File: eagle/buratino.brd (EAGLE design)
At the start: 25.4 x 50.8 mm, 50 parts, among them IC1 LTC3105MS, J2 AVR_SPI, J4 Ext Battery, Q2 2n7002PW, U4 ATMEGA256RFR2, U7 SWITCH, U8 LED-RGB, X1 16MHz, X2 32.768k, Y1 ANTENNA2SMD5

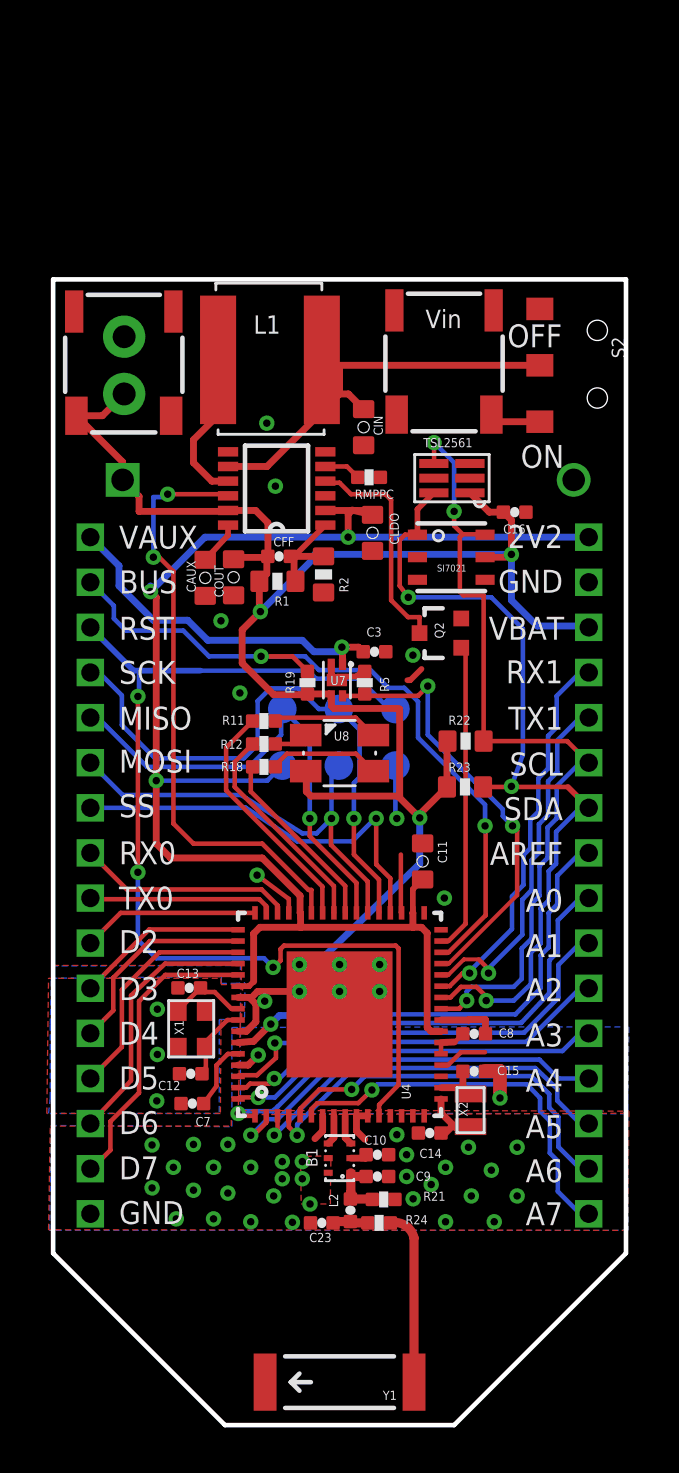
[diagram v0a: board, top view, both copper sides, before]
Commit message: replace ICSP with JTAG
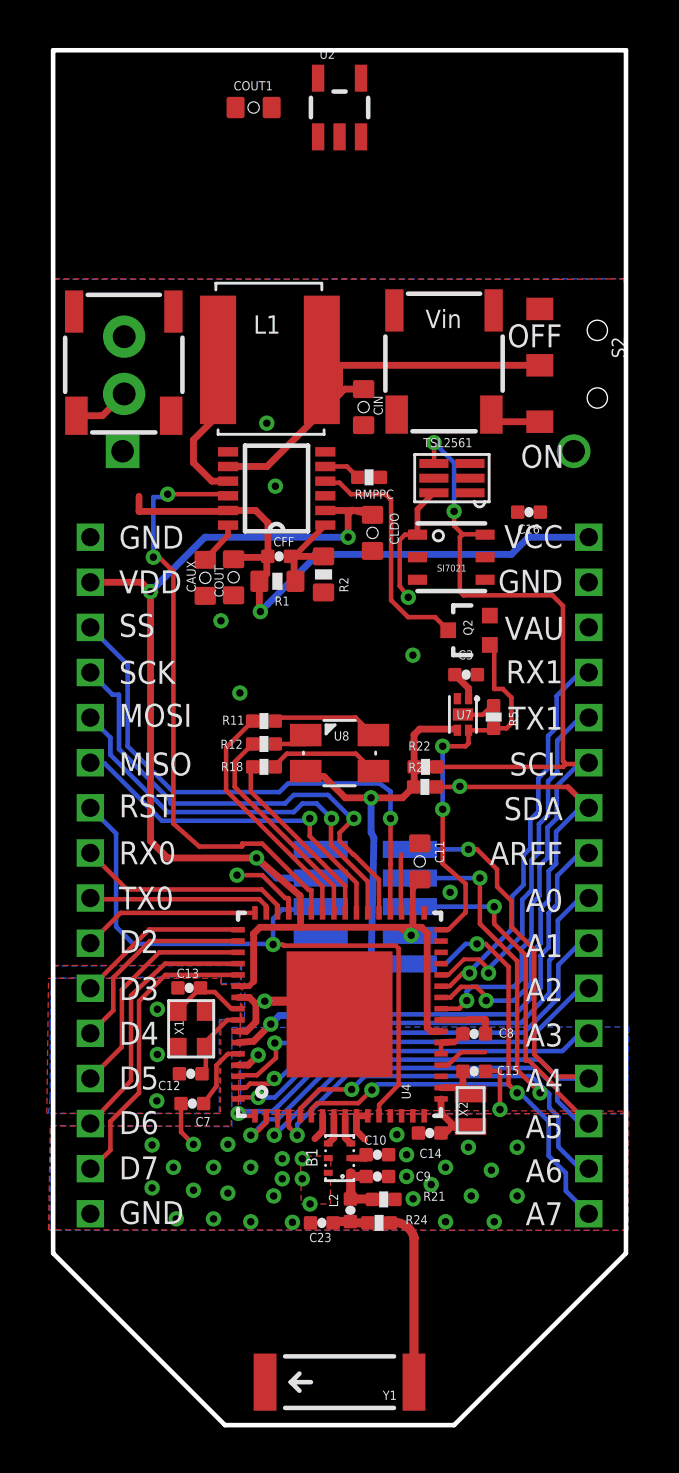
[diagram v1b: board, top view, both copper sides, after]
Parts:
- removed J2: AVR_SPI, Pinoccio:2X3-PAD
- removed R19: 2K, Pinoccio:0402-RES
- added COUT1: 1.0uF, Pinoccio:0603-CAP
- added U2: TPS78222, Pinoccio:SOT23-5
- added X3: AVR_JTAG, 620-Misc:PHB_1MM27_2X05_SNS
- R22, R23: device Pinoccio:0603-RES -> Pinoccio:0402-RES
- moved R5 5.91 mm to (19.5, 31.4)
- moved U7 5.79 mm to (18.8, 32.3)
- moved C3 4.19 mm to (18.3, 33.3)
- moved R22 2.11 mm to (16.5, 29.2)
- moved R23 1.78 mm to (16.5, 28.3)
- moved Q2 1.28 mm to (18.4, 35.2)
- moved CSTOR 1.27 mm to (13.1, 43.2)
- moved CIN 0.89 mm to (13.8, 45.1)
- moved C16 0.64 mm to (21.1, 40.5)
- moved C11 0.13 mm to (16.3, 25.0)
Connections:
- removed net BKPK-BUS: JP-L.P$2, R19.2, U4.30
- removed net BKPKVCC-EN: R5.1, U4.29, U7.P$4
- new net N$66: U2.1, U2.3
- net A4: now also X3.1
- net A5: now also X3.5
- net A6: now also X3.3
- net A7: now also X3.9
- net GND: now also COUT1.2, JP-L.P$1, U2.2, U2.4, X3.10, X3.2; no longer J2.6
- net MISO: now also JP-L.P$6; no longer J2.1, JP-L.P$5
- net MOSI: now also JP-L.P$5; no longer J2.4, JP-L.P$6
- net RESET: now also JP-L.P$7, X3.6; no longer J2.5, JP-L.P$3
- net SCK: no longer J2.3
- net SHDWN: now also R5.1, U4.29, U4.32, U7.P$4; no longer U4.31
- net SSN: now also JP-L.P$3; no longer JP-L.P$7
- net VCC: now also COUT1.1, JP-R.P$1, U2.5; no longer C16.1, JP-R.P$3, R19.1, SI7021.5, TSL2561.1
- net VCC-AE: now also C16.1, JP-R.P$3, SI7021.5, TSL2561.1; no longer JP-L.P$1
- net VDD: now also JP-L.P$2, X3.4, X3.7; no longer J2.2, JP-R.P$1
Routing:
- net BKPK-BUS: track 32.8 -> 0.00 mm, vias 2 -> 0
- net VCC: track 82.2 -> 55.7 mm, vias 4 -> 3
- net BKPKVCC-EN: track 19.7 -> 0.00 mm, vias 2 -> 0
- net RESET: track 47.6 -> 29.9 mm, vias 3 -> 1
- net A4: track 16.6 -> 32.6 mm, vias 1 -> 2
- net A5: track 16.8 -> 31.9 mm, vias 1 -> 2
- net VCC-AE: track 15.7 -> 1.32 mm, vias 1 -> 0
- net A6: track 16.5 -> 30.6 mm, vias 1 -> 3
- net SDA: track 37.8 -> 27.1 mm
- net A7: track 17.4 -> 27.7 mm, vias 1 -> 3
- net VDD: track 69.4 -> 60.9 mm, vias 3 -> 4
- net SCL: track 37.2 -> 43.3 mm
- net SSN: track 18.1 -> 24.1 mm
- net MISO: track 21.5 -> 15.9 mm
- net SCK: track 26.1 -> 21.4 mm
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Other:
- board size 25.4 x 50.8 mm -> 25.4 x 61 mm
- board text added: "Buratino v1.1"
- board text added: "VAU"
- board text added: "VCC"
- board text added: "VDD"
- board text removed: "2V2"
- board text removed: "BUS"
- board text removed: "Buratino v1.0a"
- board text removed: "VAUX"
- board text removed: "VBAT"

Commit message: replace 2mm headers with 0.1" headers
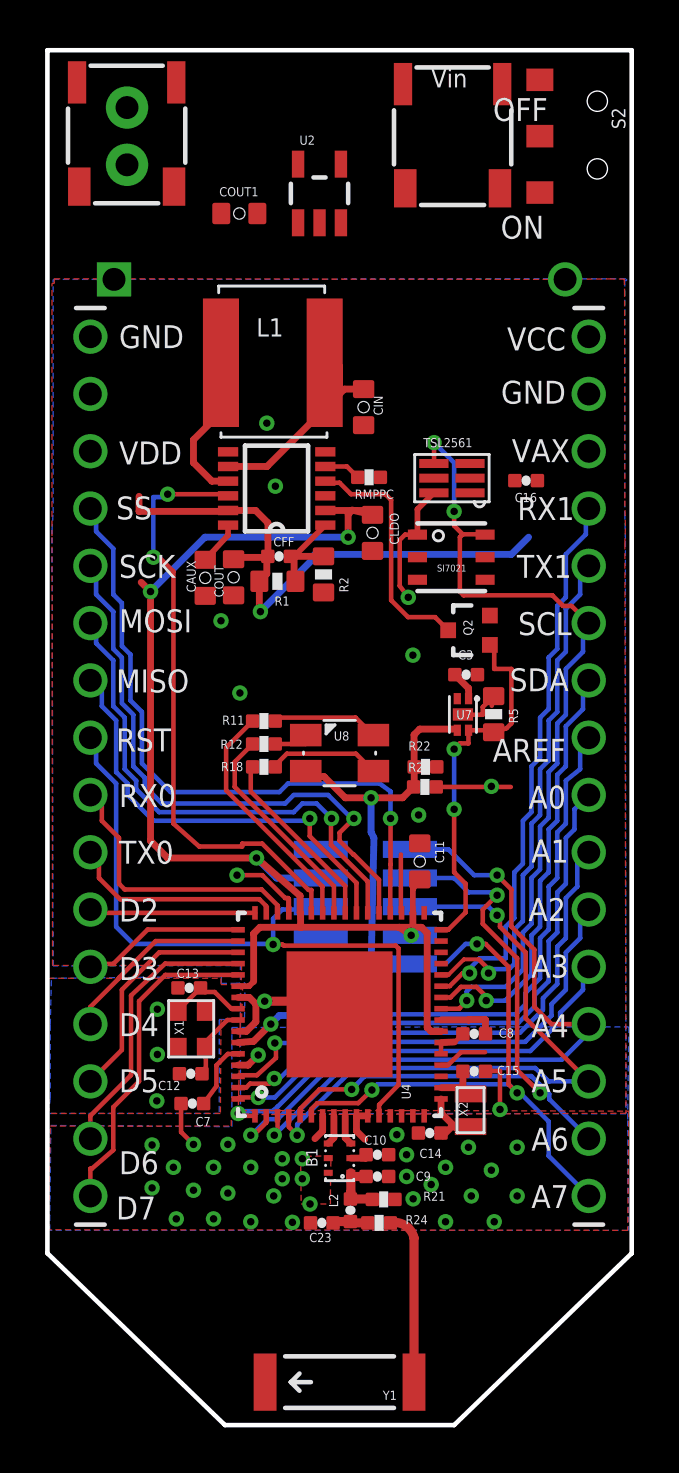
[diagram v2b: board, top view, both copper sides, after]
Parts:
- JP-L, JP-R: value M162MM -> M16PTH; device Pinoccio:1X16_2MM -> 620-Misc:1X16
- R5: device Pinoccio:0402-RES -> Pinoccio:0603-RES
- moved BATT 10.2 mm to (0.66, 60.3)
- moved J4 10.2 mm to (3.28, 58.4)
- moved S2 10.2 mm to (24.1, 57.1)
- moved PV 10.0 mm to (15.1, 60.2)
- moved JP-L 8.89 mm to (1.65, 48.3)
- moved JP-R 8.89 mm to (23.7, 48.3)
- moved CSTOR 7.63 mm to (12.7, 50.8)
- moved COUT1 4.74 mm to (8.26, 53.7)
- moved U2 3.91 mm to (11.8, 54.6)
- moved C16 1.40 mm to (21.0, 41.9)
- moved L1 0.18 mm to (9.74, 47.1)
- moved R5 0.13 mm to (19.5, 31.5)
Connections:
- new net 123: JP-L.2
- net A0: now also JP-R.9; no longer JP-R.P$9
- net A1: now also JP-R.10; no longer JP-R.P$10
- net A2: now also JP-R.11; no longer JP-R.P$11
- net A3: now also JP-R.12; no longer JP-R.P$12
- net A4: now also JP-R.13; no longer JP-R.P$13
- net A5: now also JP-R.14; no longer JP-R.P$14
- net A6: now also JP-R.15; no longer JP-R.P$15
- net A7: now also JP-R.16; no longer JP-R.P$16
- net AREF: now also JP-R.8; no longer JP-R.P$8
- net D2: now also JP-L.11; no longer JP-L.P$10
- net D3: now also JP-L.12; no longer JP-L.P$11
- net D4: now also JP-L.13; no longer JP-L.P$12
- net D5: now also JP-L.14; no longer JP-L.P$13
- net D6: now also JP-L.15; no longer JP-L.P$14
- net D7: now also JP-L.16; no longer JP-L.P$15
- net GND: now also JP-L.1, JP-R.2; no longer JP-L.P$1, JP-L.P$16, JP-R.P$2
- net MISO: now also JP-L.7; no longer JP-L.P$6
- net MOSI: now also JP-L.6; no longer JP-L.P$5
- net RESET: now also JP-L.8; no longer JP-L.P$7
- net RX0: now also JP-L.9; no longer JP-L.P$8
- net RX1: now also JP-R.4; no longer JP-R.P$4
- net SCK: now also JP-L.5; no longer JP-L.P$4
- net SCL: now also JP-R.6; no longer JP-R.P$6
- net SDA: now also JP-R.7; no longer JP-R.P$7
- net SSN: now also JP-L.4; no longer JP-L.P$3
- net TX0: now also JP-L.10; no longer JP-L.P$9
- net TX1: now also JP-R.5; no longer JP-R.P$5
- net VCC: now also JP-R.1; no longer JP-R.P$1
- net VCC-AE: now also JP-R.3; no longer JP-R.P$3
- net VDD: now also JP-L.3; no longer JP-L.P$2
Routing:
- net N$9: track 19.2 -> 9.97 mm
- net RX1: track 17.3 -> 25.0 mm
- net TX1: track 16.1 -> 23.2 mm
- net SCL: track 43.3 -> 36.6 mm
- net SSN: track 24.1 -> 29.5 mm
- net VCC: track 55.7 -> 50.5 mm
- net AREF: track 22.6 -> 27.5 mm
- net SCK: track 21.4 -> 26.1 mm
- net MOSI: track 18.2 -> 22.6 mm
- net A0: track 20.7 -> 25.0 mm
- net A1: track 19.3 -> 23.0 mm
- net MISO: track 15.9 -> 19.4 mm
- net A2: track 18.6 -> 21.9 mm
- net A5: track 31.9 -> 28.8 mm
- net RESET: track 29.9 -> 33.0 mm
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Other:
- board size 25.4 x 61 mm -> 25.9 x 61 mm
- board text added: "VAX"
- board text removed: "VAU"

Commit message: add PIR
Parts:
- removed PV: SolarCell, bean:JST-SFH
- added J1: Vcc-Vdd Tie, Pinoccio:SJ_2S-NO
- added J2: Ext Battery, Pinoccio:1X02
- added R3: 10K, Pinoccio:0603-RES
- added R4: 47K, Pinoccio:0603-RES
- added S1: (no value), SparkFun-Electromechanical:TACTILE-PTH
- added U$1: IRS-B210ST01R1, 620-Sensors:PIRSMT
- added VIN1: Ext Power, bean:JST-SFH
- BATT: value JST Bat -> Aux Bat
- J4: value Ext Battery -> Aux Batt
- R11, R12, R18, R22, R23: device Pinoccio:0402-RES -> Pinoccio:0603-RES
- moved COUT1 8.50 mm to (9.65, 45.3), turned to 180 degrees
- moved U2 6.91 mm to (9.78, 48.0), turned to 180 degrees
- moved S2 1.40 mm to (24.0, 55.8)
- moved BATT 1.17 mm to (0.41, 59.1)
- moved CIN 1.02 mm to (13.8, 44.1)
- moved J4 0.92 mm to (3.02, 57.5)
- moved R22 0.74 mm to (16.9, 29.8)
- moved R11 0.65 mm to (8.71, 31.3)
- moved R12 0.64 mm to (8.71, 30.2)
- moved R23 0.54 mm to (16.9, 28.7)
- moved R18 0.52 mm to (8.84, 29.1)
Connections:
- removed net 123: JP-L.2
- removed net N$66: U2.1, U2.3
- removed net N$9: CIN.1, IC1.8, L1.P$1, S2.2
- new net BTN: R3.2, S1.3, S1.4, U4.32
- new net VIN: CIN.1, IC1.8, L1.P$1, S2.2, U2.1, U2.3
- net A0: now also R4.1, U$1.VOUT
- net GND: now also J2.1, R4.2, S1.1, S1.2, U$1.GND, U$1.GND*1, U$1.GND*2, VIN1.2; no longer PV.2
- net N$24: now also J2.2, VIN1.1; no longer PV.1
- net SHDWN: now also U4.31; no longer U4.29, U4.32
- net VCC: now also J1.1, JP-L.3
- net VDD: now also J1.2, JP-L.2, R3.1, U$1.VIN; no longer JP-L.3
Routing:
- net BTN: track 0.00 -> 60.6 mm, vias 0 -> 2
- net VIN: track 0.00 -> 34.9 mm
- net VCC: track 50.5 -> 83.3 mm
- net VDD: track 58.6 -> 76.8 mm
- net N$9: track 9.97 -> 0.00 mm
- net N$24: track 0.00 -> 4.77 mm
- net A0: track 25.0 -> 26.2 mm
- net LED-GRN: track 10.8 -> 11.6 mm
- net SDA: track 28.5 -> 27.7 mm
- net N$1: track 1.75 -> 2.46 mm
- net LED-RED: track 9.65 -> 10.3 mm
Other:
- board size 25.9 x 61 mm -> 25.9 x 59.9 mm

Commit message: pre-fab
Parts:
- added U$2: LOGO-OSHWSILKSCREEN, Pinoccio:LOGO-OSHW-SS
- C16, C3, CFF: device Pinoccio:0402-CAP -> Pinoccio:0603-CAP
- RMPPC: device Pinoccio:0402-RES -> Pinoccio:0603-RES
- S1: value (none) -> BTN
- moved R22 6.02 mm to (21.0, 34.3)
- moved R23 5.18 mm to (21.1, 31.7)
- moved R5 1.71 mm to (18.4, 30.3)
- moved C3 1.63 mm to (17.0, 32.3), turned to 180 degrees
- moved U7 1.63 mm to (17.5, 31.3)
- moved Q2 1.53 mm to (17.3, 34.2)
- moved COUT1 0.65 mm to (9.78, 46.0)
- moved U2 0.51 mm to (9.78, 48.5)
- moved RMPPC 0.36 mm to (14.3, 42.3)
- renumbered U$1 to PIR
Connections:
- net VCC: no longer JP-R.1
- net VIN: now also JP-R.1
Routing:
- net VCC-AE: track 1.32 -> 24.5 mm, vias 0 -> 2
- net A0: track 26.2 -> 43.7 mm, vias 1 -> 3
- net SDA: track 27.7 -> 37.1 mm, vias 3 -> 1
- net VIN: track 34.9 -> 41.9 mm
- net SCL: track 36.6 -> 39.1 mm
- net N$21: track 10.8 -> 12.3 mm
- net GND: track 28.4 -> 29.8 mm, vias 45 -> 47
- net SHDWN: track 16.7 -> 15.4 mm, vias 2 -> 0
- net VCC: track 83.3 -> 82.4 mm, vias 3 -> 6
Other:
- board text added: "Buratino v0.2"
- board text added: "Engineered in Arlington, VA USA"
- board text added: "VIN"
- board text removed: "Buratino v1.1"

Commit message: add BOM, final tweaks
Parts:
- added J3: Vaux-Vcc Tie, Pinoccio:SJ_2S-NO
- C12, C13, C14, C15: value 12pF -> 10pF
- C7, C8: device Pinoccio:0402-CAP -> Pinoccio:0603-CAP
- CIN: device Pinoccio:0603-CAP -> Pinoccio:0805
- moved CIN 0.92 mm to (14.0, 45.0)
- moved C8 0.36 mm to (18.9, 17.1)
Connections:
- net VCC: now also J3.2
- net VCC-AE: now also J3.1
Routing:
- net VCC: track 82.4 -> 83.9 mm
- net VCC-AE: track 24.5 -> 25.5 mm
